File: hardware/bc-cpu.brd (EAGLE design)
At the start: 87.6 x 73.7 mm, 86 parts, among them J1 BATTERIES, J2 PHT, J3 LED Matrix, J5 BRK5, U1 R-735.0P, U2 MAX11632EEG+, U3 MAX11632EEG+, U4 AD1584BRTZ

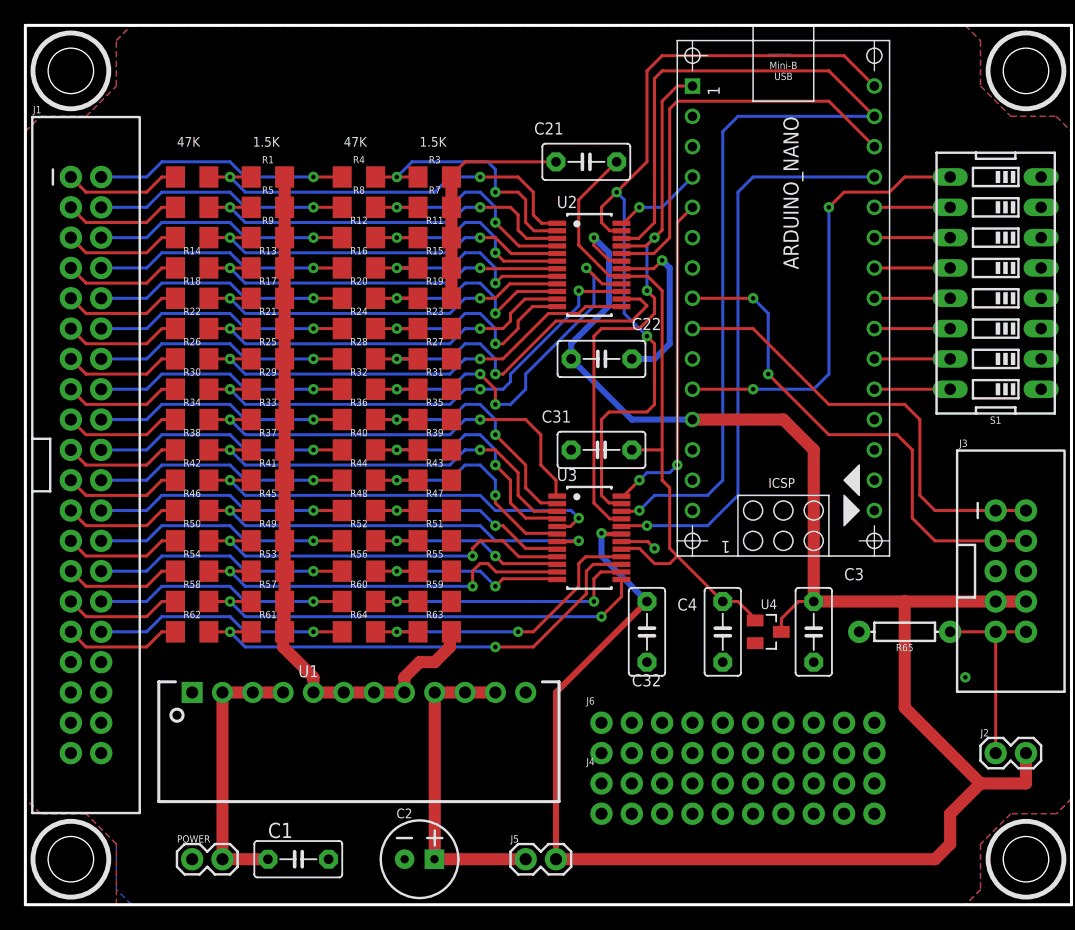
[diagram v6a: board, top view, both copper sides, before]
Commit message: Text, labels, positioning
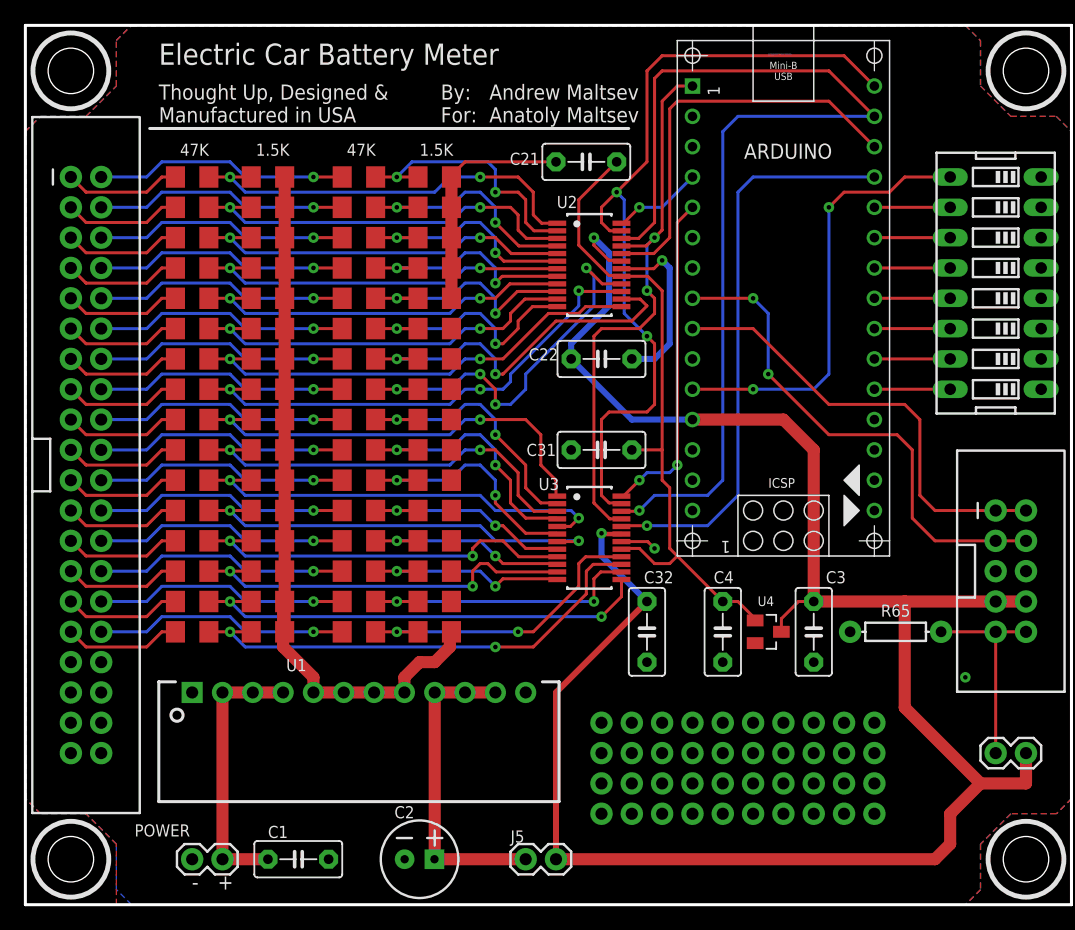
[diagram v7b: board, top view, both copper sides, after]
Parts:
- J2: value PHT -> PHOTO
- J3: value LED Matrix -> LED MATRIX
- R65: value (none) -> 10K
- S1: value Options -> OPTIONS
- moved R65 0.76 mm to (72.9, 22.9)
- renumbered ARDUINO_NANO to ARDUINO
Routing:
- net PHOTO: track 16.5 -> 17.3 mm
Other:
- board text added: "+"
- board text added: "-"
- board text added: "Andrew Maltsev Anatoly Maltsev"
- board text added: "By: For:"
- board text added: "Electric Car Battery Meter"
- board text added: "Thought Up, Designed & Manufactured in USA"

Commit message: Power input adjustments
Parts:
- added GND, V12: WIREPAD3,17/1,2, wirepad:3,17/1,2
- POWER: value 12V -> 7...18V
- moved C1 2.84 mm to (24.1, 6.35)
- moved C2 2.84 mm to (35.6, 5.08)
- moved POWER 2.54 mm to (14.0, 6.35)
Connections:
- net GND: now also GND.1
- net VCC: now also V12.1
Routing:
- net GND: track 100.8 -> 136.9 mm
- net VCC: track 22.9 -> 30.0 mm
- net N$11: track 26.7 -> 23.4 mm
- added copper zone on layer 1, net N$2
- added copper zone on layer 16, net N$3
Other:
- board text added: "6...18V"
